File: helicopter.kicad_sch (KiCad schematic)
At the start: 7 parts, among them U1 STM32F746ZGTx

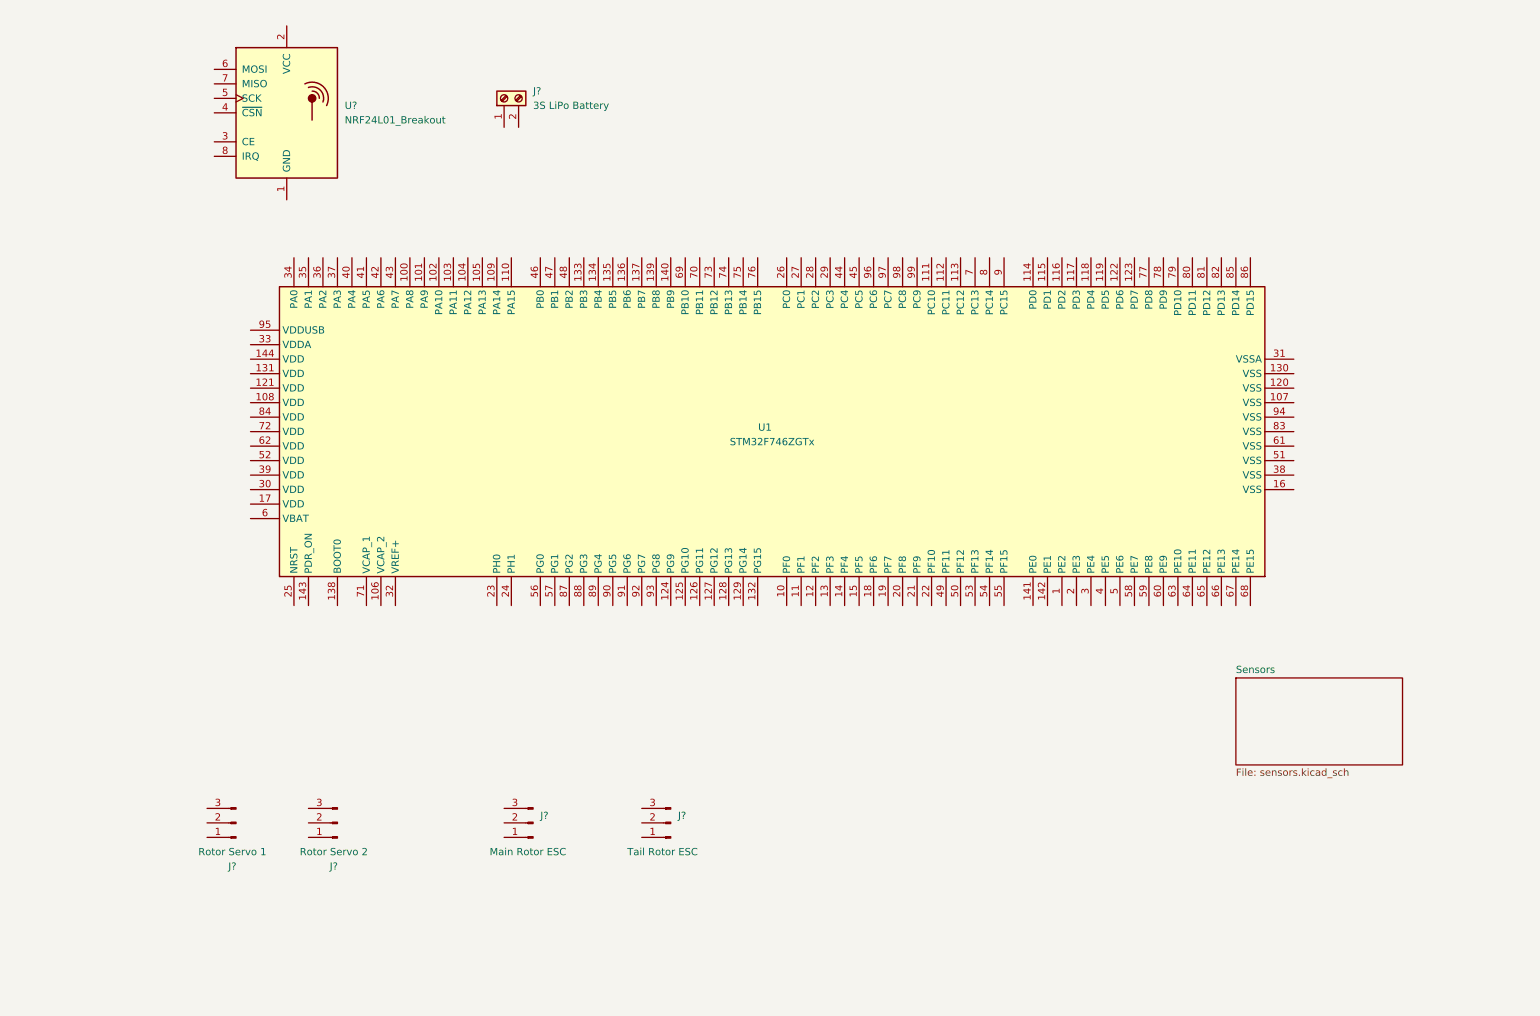
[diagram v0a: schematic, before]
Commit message: add functions for sd-card/ems/nrf24
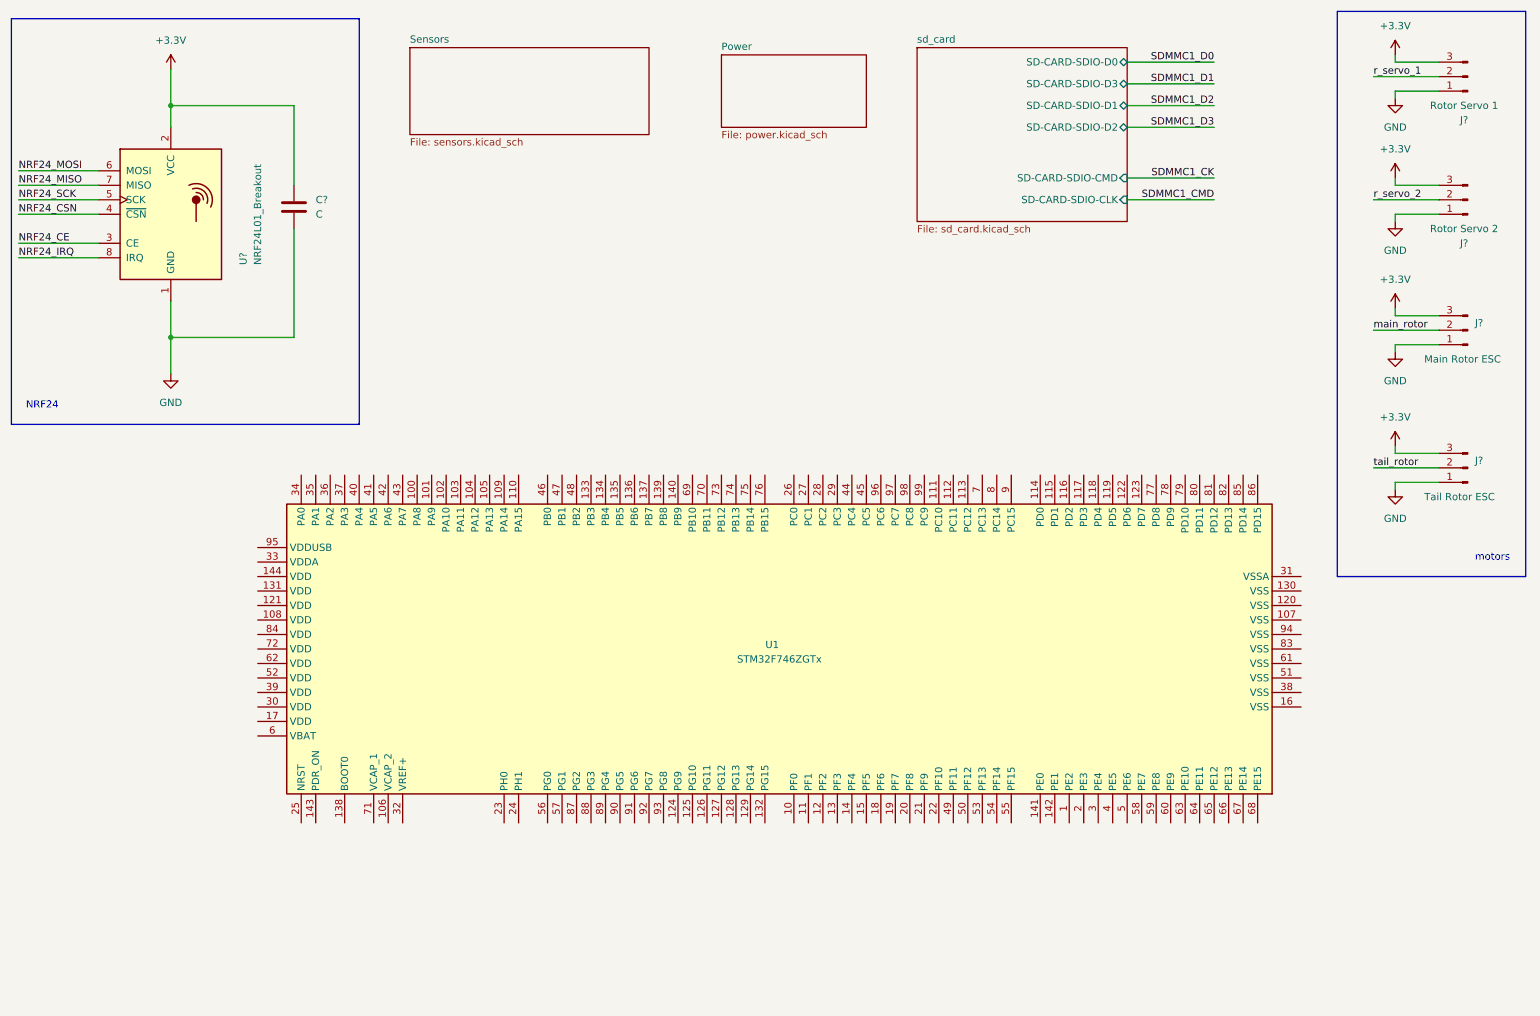
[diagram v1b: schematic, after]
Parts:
- removed J?: 3S LiPo Battery, symbol Connector:Screw_Terminal_01x02
- added C?: C, symbol Device:C
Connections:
- net GND: now reaches J?.1 (Pin_1)
- net GND: now also J?.1 (Pin_1), J?.1 (Pin_1), J?.1 (Pin_1), U?.1 (GND), C?.2
- net r_servo_1: now reaches J?.2 (Pin_2)
- net +3.3V: now reaches J?.3 (Pin_3)
- net +3.3V: now also J?.3 (Pin_3), J?.3 (Pin_3), J?.3 (Pin_3), U?.2 (VCC), C?.1
- net NRF24_CE: now reaches U?.3 (CE)
- net NRF24_CSN: now reaches U?.4 (~{CSN})
- net NRF24_SCK: now reaches U?.5 (SCK)
- net NRF24_MOSI: now reaches U?.6 (MOSI)
- net NRF24_MISO: now reaches U?.7 (MISO)
- net NRF24_IRQ: now reaches U?.8 (IRQ)
- net tail_rotor: now reaches J?.2 (Pin_2)
- net main_rotor: now reaches J?.2 (Pin_2)
- net r_servo_2: now reaches J?.2 (Pin_2)
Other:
- added sheet Power (power.kicad_sch)
- added sheet sd_card (sd_card.kicad_sch)
- note added: "NRF24"
- note added: "motors"
- moved on the sheet: J?, U1, U?

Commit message: Refactor the mainboard
- Use smaller STM
- Use MPU-9250 as a motion sensor
- Connect some peripherals to the MCU
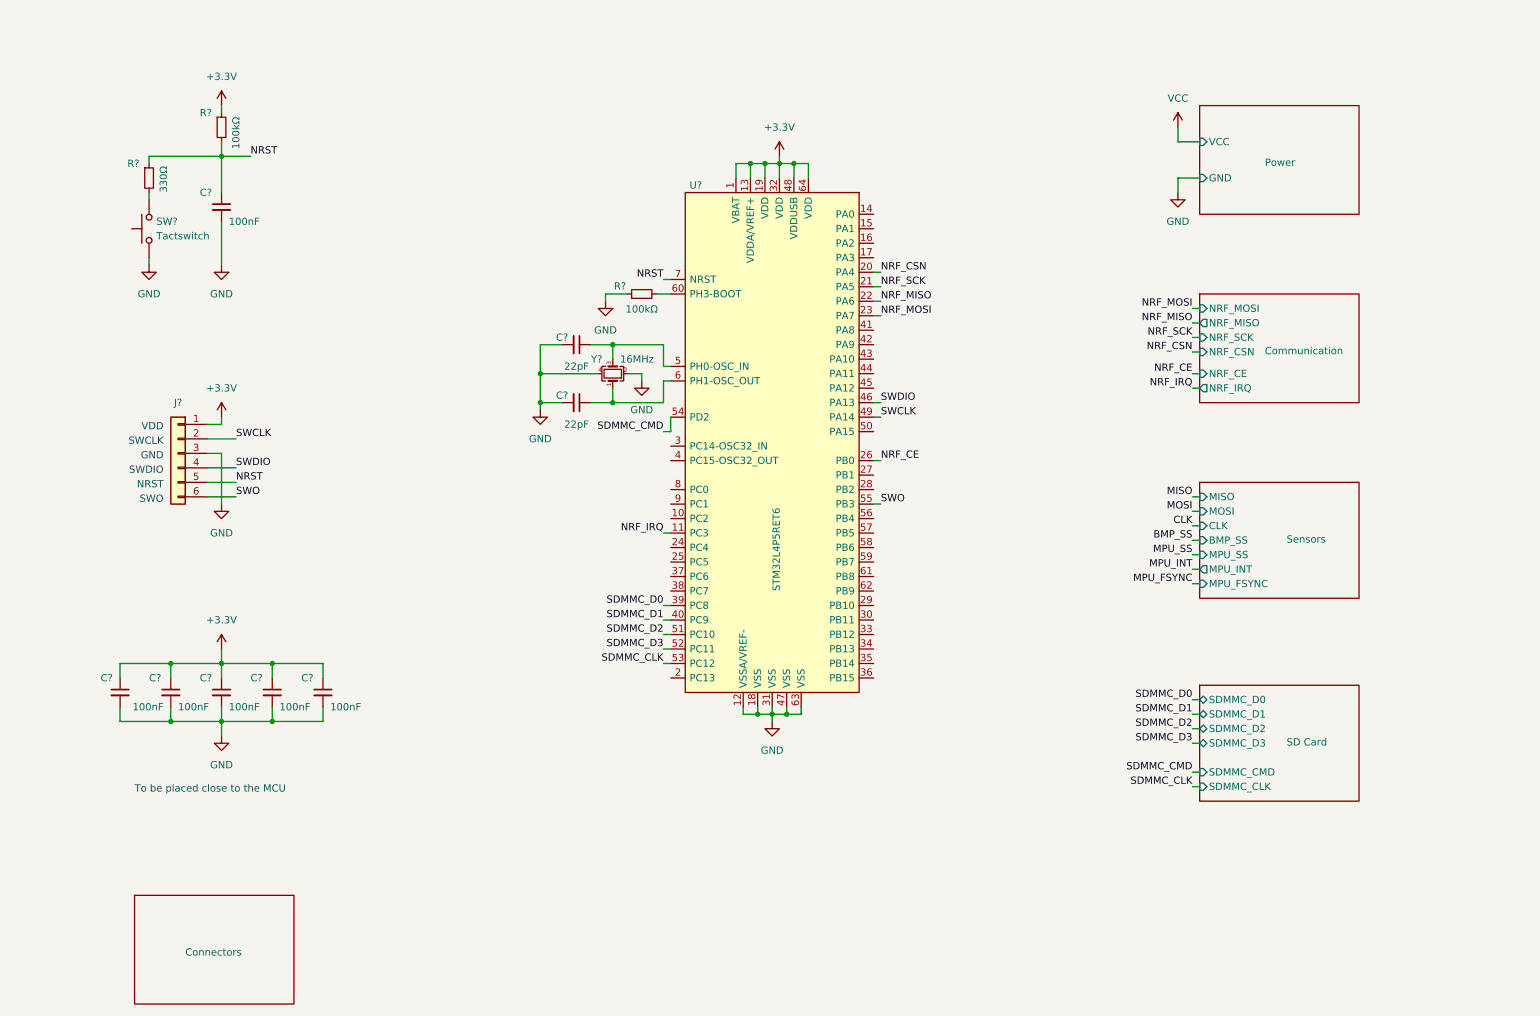
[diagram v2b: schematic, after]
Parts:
- removed C?: C, symbol Device:C
- removed J?: Rotor Servo 1, symbol Connector:Conn_01x03_Male
- removed J?: Tail Rotor ESC, symbol Connector:Conn_01x03_Male
- removed J?: Main Rotor ESC, symbol Connector:Conn_01x03_Male
- removed J?: Rotor Servo 2, symbol Connector:Conn_01x03_Male
- removed U1: STM32F746ZGTx, Package_QFP:LQFP-144_20x20mm_P0.5mm, symbol MCU_ST_STM32F7:STM32F746ZGTx
- removed U?: NRF24L01_Breakout, RF_Module:nRF24L01_Breakout, symbol RF:NRF24L01_Breakout
- added C? (x6): 100nF, Capacitor_SMD:C_0603_1608Metric, symbol Device:C_Small
- added C? (x2): 22pF, Capacitor_SMD:C_0603_1608Metric, symbol Device:C_Small
- added J?: Conn_01x06, Connector_PinHeader_2.54mm:PinHeader_1x06_P2.54mm_Vertical_SMD_Pin1Left, symbol Connector_Generic:Conn_01x06
- added R?: 330Ω, Resistor_SMD:R_0603_1608Metric, symbol Device:R_Small
- added R? (x2): 100kΩ, Resistor_SMD:R_0603_1608Metric, symbol Device:R_Small
- added SW?: Tactswitch, Button_Switch_SMD:SW_SPST_PTS645, symbol Switch:SW_Push
- added U?: STM32L4P5RET6, Package_QFP:LQFP-64_10x10mm_P0.5mm, symbol Local_Library:STM32L4P5RET6
- added Y?: 16MHz, Crystal:Crystal_SMD_3225-4Pin_3.2x2.5mm, symbol Device:Crystal_GND24_Small
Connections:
- net +3.3V: now also C?.1, C?.1, C?.1, C?.1, C?.1, J?.1 (Pin_1), R?.1, U?.1 (VBAT), U?.13 (VDDA/VREF+), U?.19 (VDD), U?.32 (VDD), U?.48 (VDDUSB), U?.64 (VDD)
- net GND: now also C?.2, C?.2, C?.2, C?.2, C?.2, C?.2, C?.2, C?.2, J?.3 (Pin_3), R?.1, SW?.1, U?.12 (VSSA/VREF-), U?.18 (VSS), U?.31 (VSS), U?.47 (VSS), U?.63 (VSS), Y?.2, Y?.4
- new net: R?.2, SW?.2
- new net: C?.1, U?.6 (PH1-OSC_OUT), Y?.1
- new net: C?.1, U?.5 (PH0-OSC_IN), Y?.3
- new net: R?.2, U?.60 (PH3-BOOT)
- new net NRF_CE: U?.26 (PB0)
- new net NRF_CSN: U?.20 (PA4)
- new net NRF_IRQ: U?.11 (PC3)
- new net NRF_MISO: U?.22 (PA6)
- new net NRF_MOSI: U?.23 (PA7)
- new net NRF_SCK: U?.21 (PA5)
- new net NRST: C?.1, J?.5 (Pin_5), R?.1, R?.2, U?.7 (NRST)
- new net SDMMC_CLK: U?.53 (PC12)
- new net SDMMC_CMD: U?.54 (PD2)
- new net SDMMC_D0: U?.39 (PC8)
- new net SDMMC_D1: U?.40 (PC9)
- new net SDMMC_D2: U?.51 (PC10)
- new net SDMMC_D3: U?.52 (PC11)
- new net SWCLK: J?.2 (Pin_2), U?.49 (PA14)
- new net SWDIO: J?.4 (Pin_4), U?.46 (PA13)
- new net SWO: J?.6 (Pin_6), U?.55 (PB3)
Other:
- sheet sd_card renamed SD Card
- added sheet Communication (communication.kicad_sch)
- added sheet Connectors (connectors.kicad_sch)
- sheet Power ports: added GND, VCC; removed none
- sheet SD Card ports: added SDMMC_CLK, SDMMC_CMD, SDMMC_D0, SDMMC_D1, SDMMC_D2, SDMMC_D3; removed SD-CARD-SDIO-CLK, SD-CARD-SDIO-CMD, SD-CARD-SDIO-D0, SD-CARD-SDIO-D1, SD-CARD-SDIO-D2, SD-CARD-SDIO-D3
- sheet Sensors ports: added BMP_SS, CLK, MISO, MOSI, MPU_FSYNC, MPU_INT, MPU_SS; removed none
- note added: "GND"
- note added: "NRST"
- note added: "SWCLK"
- note added: "SWDIO"
- note added: "SWO"
- note added: "To be placed close to the MCU"
- note added: "VDD"
- note removed: "NRF24"
- note removed: "motors"

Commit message: Connect sensors to the MCU
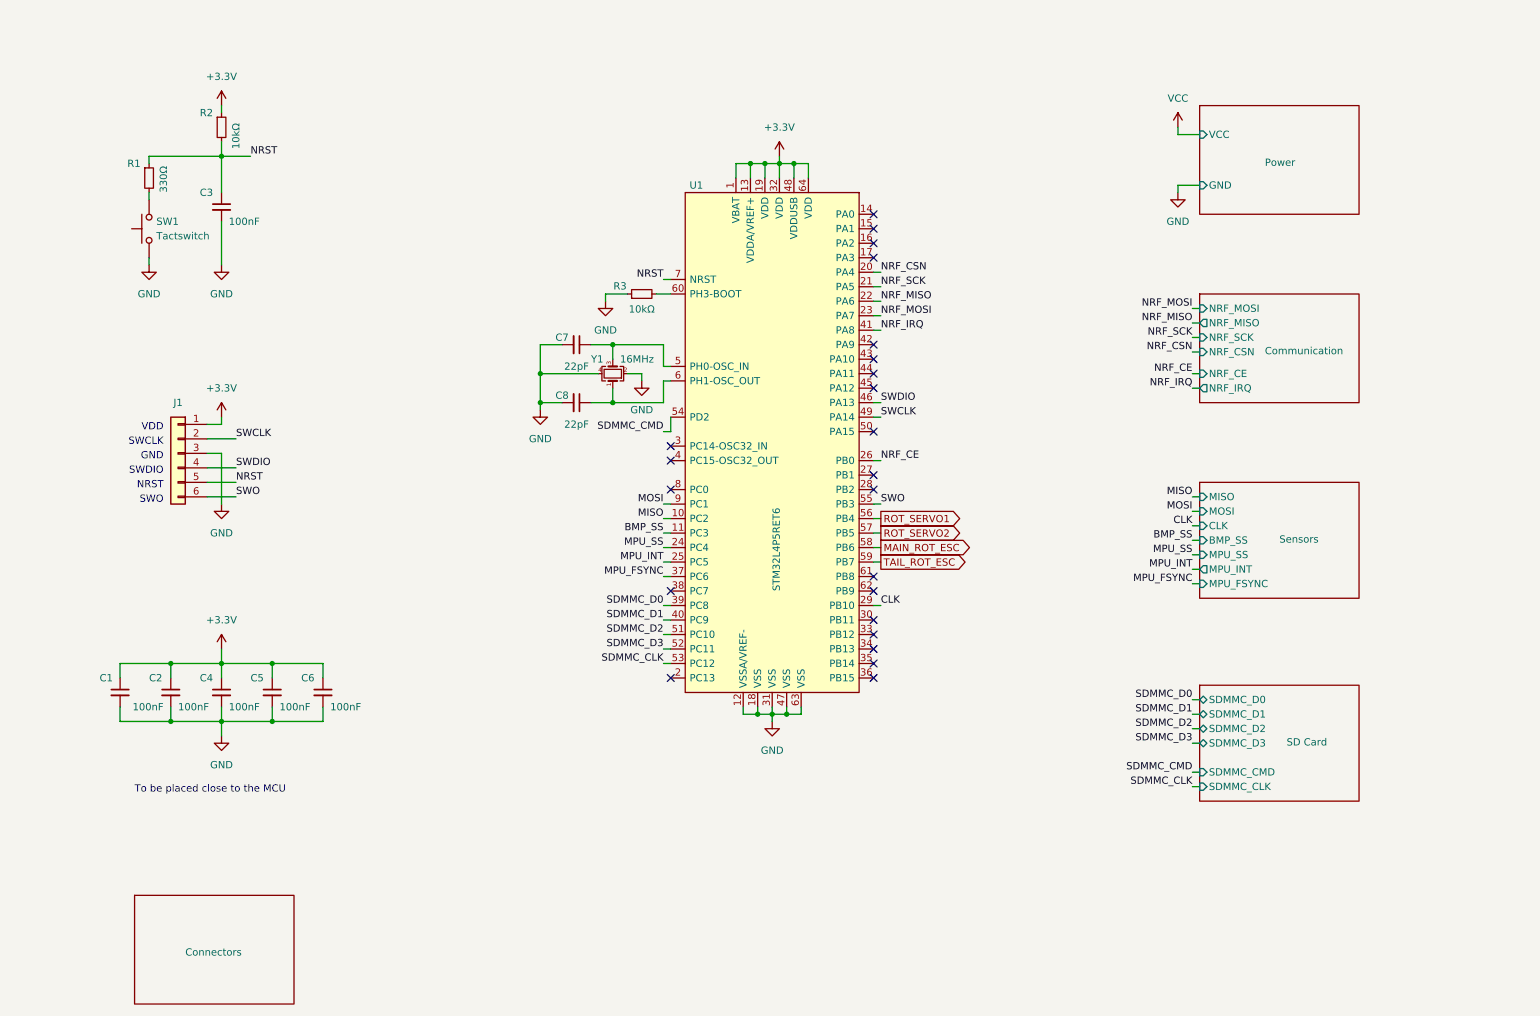
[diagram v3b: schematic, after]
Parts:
- R2, R3: renamed from R?; value 100kΩ -> 10kΩ
- gave numbers to parts that had none: 13
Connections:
- net BMP_SS: now also U1.11 (PC3)
- net CLK: now also U1.29 (PB10)
- net MISO: now also U1.10 (PC2)
- net MOSI: now also U1.9 (PC1)
- net MPU_FSYNC: now also U1.37 (PC6)
- net MPU_INT: now also U1.25 (PC5)
- net MPU_SS: now also U1.24 (PC4)
- net NRF_IRQ: now also U1.41 (PA8); no longer U1.11 (PC3)
- net ROT_SERVO1: now reaches U1.56 (PB4)
- net ROT_SERVO2: now reaches U1.57 (PB5)
- net MAIN_ROT_ESC: now reaches U1.58 (PB6)
- net TAIL_ROT_ESC: now reaches U1.59 (PB7)
- no-connect marks 0 -> 23

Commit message: Improve the power section:
- add ADC circuit to measure battery level
- add 5V LDO regulator
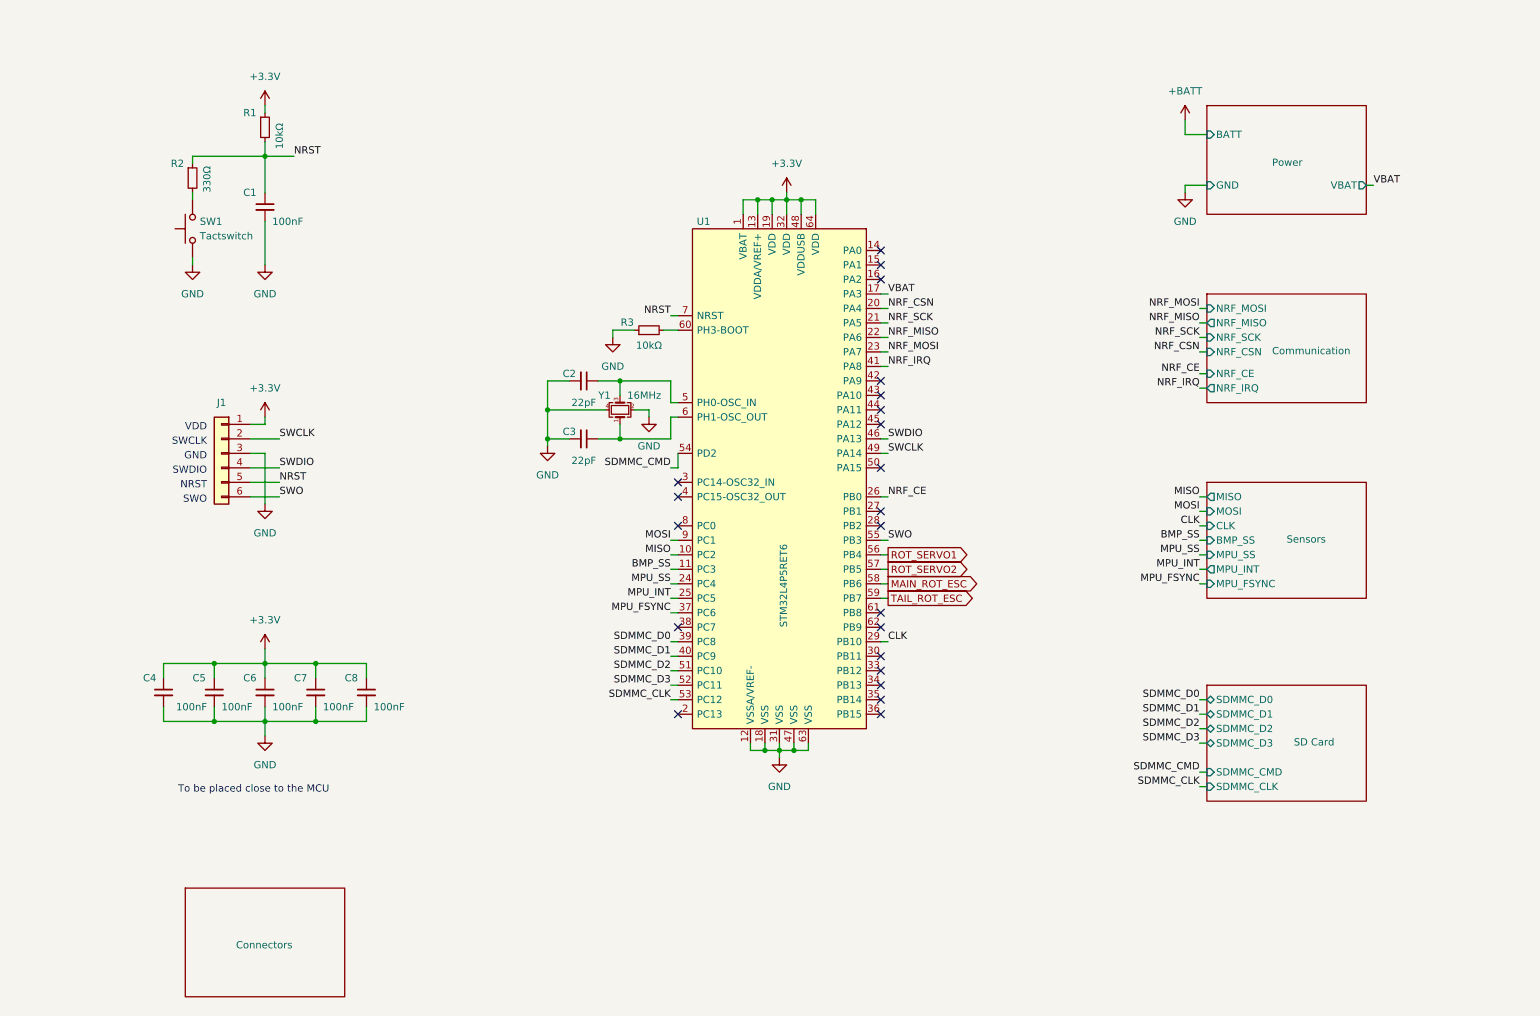
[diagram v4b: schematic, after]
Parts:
- renumbered C3 to C1, C7 to C2, C8 to C3, C1 to C4, C2 to C5, C4 to C6, C5 to C7, C6 to C8, R2 to R1, R1 to R2
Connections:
- net VBAT: now reaches U1.17 (PA3)
- no-connect marks 23 -> 22
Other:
- sheet Power ports: added BATT, VBAT; removed VCC
- moved on the sheet: C1, C2, C3, C4, C5, C6, C7, C8, J1, R1, R2, R3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
